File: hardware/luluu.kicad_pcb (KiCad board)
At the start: 4 copper layers, 64 x 30 mm, 62 parts, among them J1 BATT_CON, J2 RPi SWD, J3 STEMMA_{QT} I_{2}C, J4 Micro_SD_Card, J5 GPIO0, J6 USB_C_Receptacle_USB2.0, J7 DISP_LCD_ST7789, J8 GPIO1, Q1 AO3401A, Q2 BSS138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

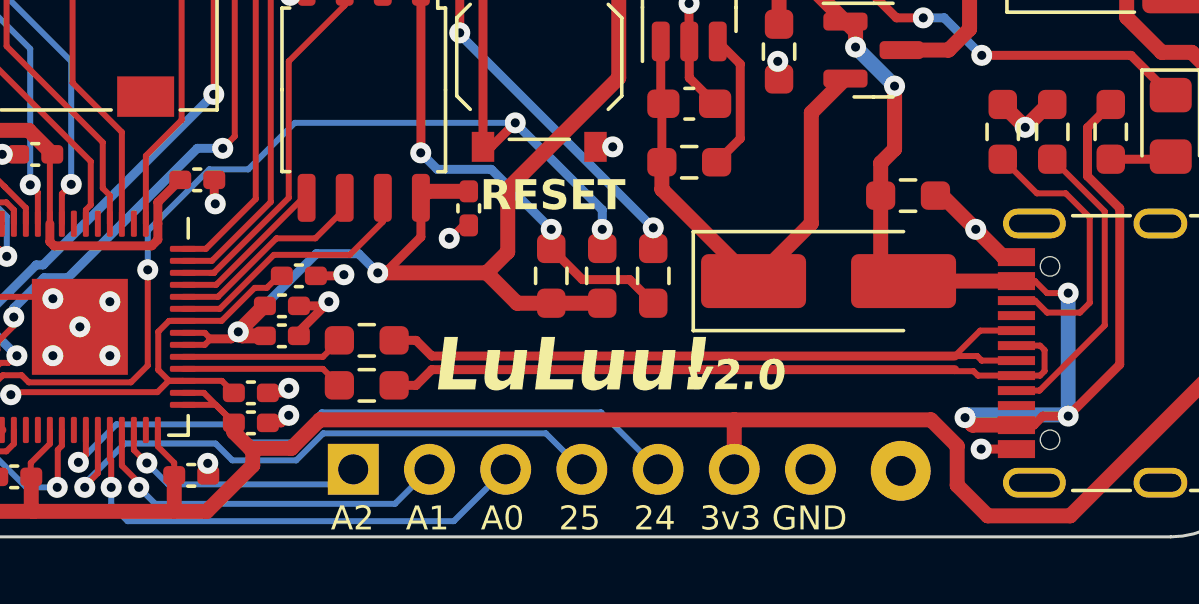
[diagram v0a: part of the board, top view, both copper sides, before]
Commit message: optimize usb routing
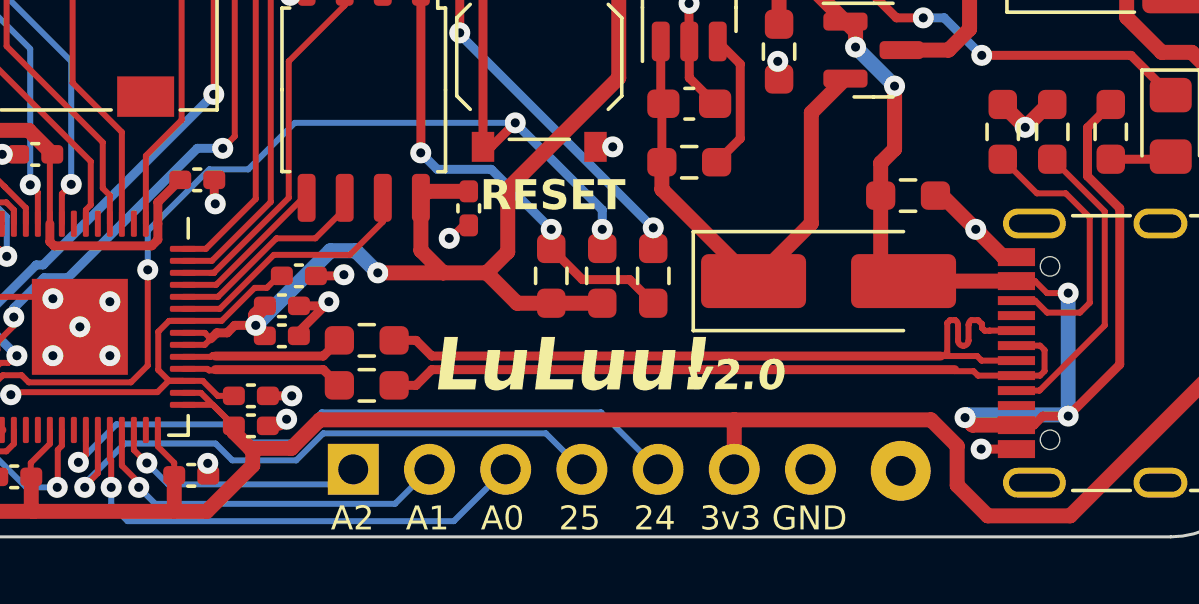
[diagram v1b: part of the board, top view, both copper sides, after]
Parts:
- moved C12 0.10 mm to (140.3, 103.8)
- moved C9 0.10 mm to (140.3, 102.8)
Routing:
- net /USB_D+: track 23.4 -> 26.3 mm
- net +3V3: track 269.8 -> 268.5 mm

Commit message: more work on v2
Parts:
- removed MNT0, MNT1, MNT2: Pin_D1.0mm_L10.0mm, Connector_Pin:Pin_D1.0mm_L10.0mm
- added H1: MH, luluu:MountingHole_1.1mm_M1, F.Cu at (101.8, 103.2)
- added H2: MH, luluu:MountingHole_1.1mm_M1, F.Cu at (162.2, 76.8)
- added H3: MH, luluu:MountingHole_1.1mm_M1, F.Cu at (152.2, 103.2)
- added H4: MH, luluu:MountingHole_1.1mm_M1, F.Cu at (130.0, 76.8)
- added H5: MH, luluu:MountingHole_1.1mm_M1, F.Cu at (118.0, 76.8)
- added JP1: SW_A_JMPER, Jumper:SolderJumper-3_P1.3mm_Bridged12_RoundedPad1.0x1.5mm, B.Cu at (139.9, 87.9)
- added JP2: SW_B_JMPER, Jumper:SolderJumper-3_P1.3mm_Bridged12_RoundedPad1.0x1.5mm, B.Cu at (140.0, 82.4)
- SW1: value SW_USBBOOT -> SW_B
- SW2: value SW_RESET -> SW_A
- moved C1 11.0 mm to (136.6, 95.5), turned to 0 degrees
- moved C16 10.6 mm to (122.9, 92.1)
- moved C11 10.3 mm to (118.4, 99.2)
- moved C10 10.3 mm to (131.9, 96.2)
- moved C12 10.3 mm to (130.3, 101.2)
- moved C13 10.3 mm to (131.4, 98.2)
- moved C14 10.3 mm to (131.4, 97.2)
- moved C15 10.3 mm to (117.7, 98.1)
- moved C18 10.3 mm to (128.6, 93.0)
- moved C19 10.3 mm to (128.3, 102.9)
- moved C2 10.3 mm to (144.9, 90.5)
- moved C20 10.3 mm to (103.8, 80.5)
- moved C21 10.3 mm to (107.0, 80.8)
- moved C22 10.3 mm to (115.3, 79.0)
- moved C3 10.3 mm to (115.5, 94.4)
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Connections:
- R16 pad 1: Net-(R16-Pad1) -> /SW_B_BOOT
- R7 pad 1: Net-(U3-RUN) -> /SW_A_RST
- SW1 pad 1: Net-(R16-Pad1) -> Net-(JP2-C)
- SW2 pad 2: Net-(U3-RUN) -> Net-(JP1-C)
- U3 pad 26: Net-(U3-RUN) -> /SW_A_RST
- U3 pad 3: unconnected-(U3-GPIO1-Pad3) -> /SW_A_GPIO
- U3 pad 8: unconnected-(U3-GPIO6-Pad8) -> /SW_B_GPIO
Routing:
- net Net-(U3-RUN): track 37.1 -> 0.00 mm, vias 3 -> 0
- net /SW_A_RST: track 0.00 -> 33.5 mm, vias 0 -> 2
- net /SW_B_GPIO: track 0.00 -> 21.0 mm, vias 0 -> 1
- net Net-(R16-Pad1): track 20.1 -> 0.00 mm, vias 4 -> 0
- net /SW_A_GPIO: track 0.00 -> 16.1 mm, vias 0 -> 1
- net /SW_B_BOOT: track 0.00 -> 14.5 mm, vias 0 -> 1
- net Net-(JP1-C): track 0.00 -> 9.54 mm, vias 0 -> 1
- net Net-(JP2-C): track 0.00 -> 9.04 mm, vias 0 -> 2
- net Net-(SW3-A): track 10.4 -> 12.1 mm
- net +3V3: track 268.5 -> 266.9 mm
- net GND: track 99.7 -> 99.1 mm
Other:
- outline, holes or cut-outs redrawn
- board text added: "A"
- board text added: "B"
- board text added: "BOOT/B"
- board text added: "RESET/A"
- board text added: "RST"
- board text added: "SWD_{RPi}"
- board text added: "|"
- board text removed: "RESET"
- board text removed: "RPi SWD"
